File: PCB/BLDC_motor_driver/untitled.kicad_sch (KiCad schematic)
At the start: 21 parts, among them Q8 CSD18533Q5A, Q9 CSD18533Q5A, U1 INA240A2D, U3 IR2104, U4 LMV393

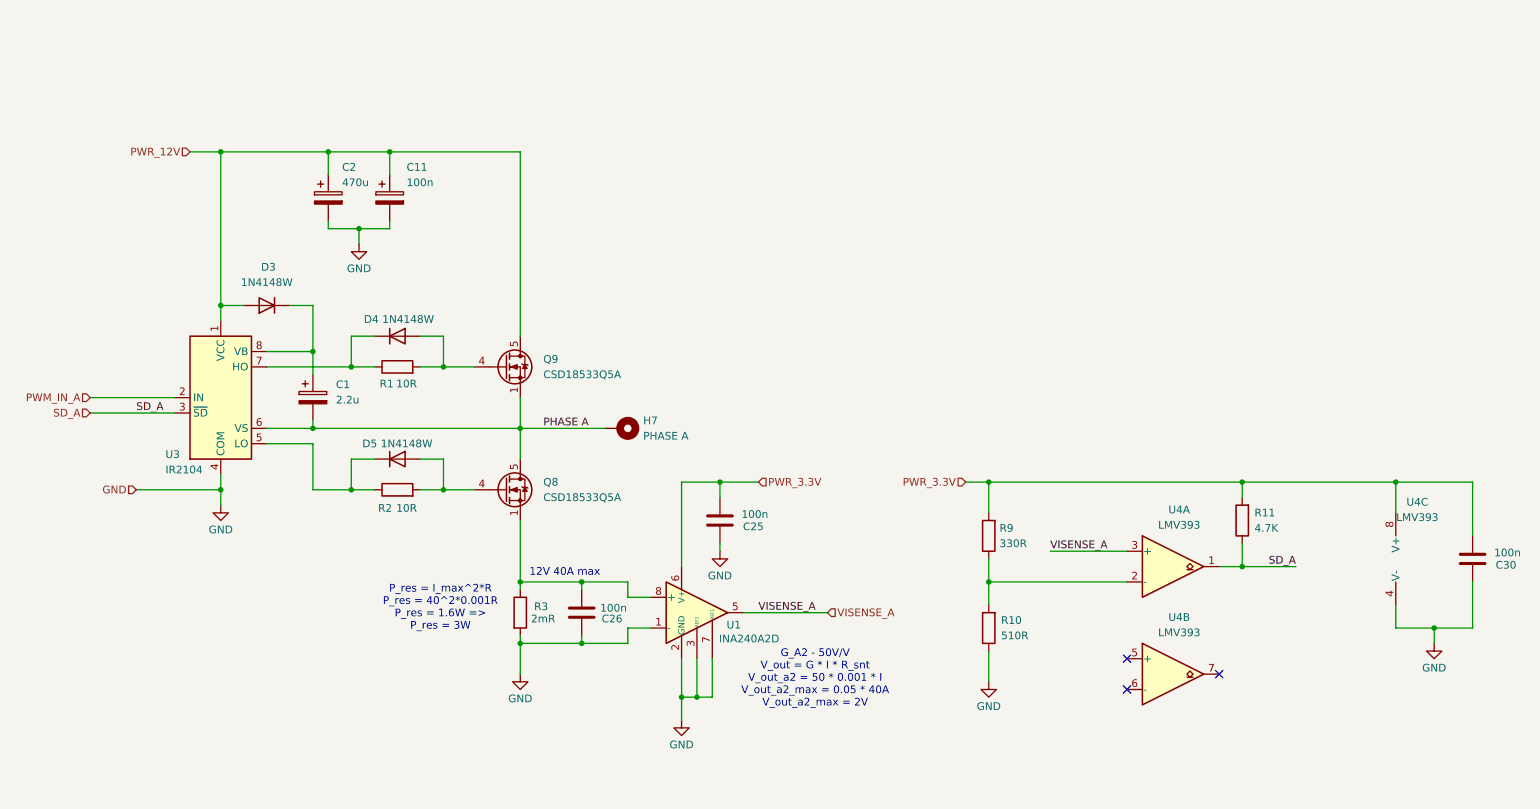
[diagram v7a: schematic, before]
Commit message: Succesfully tested phase alignment with new bldc driver
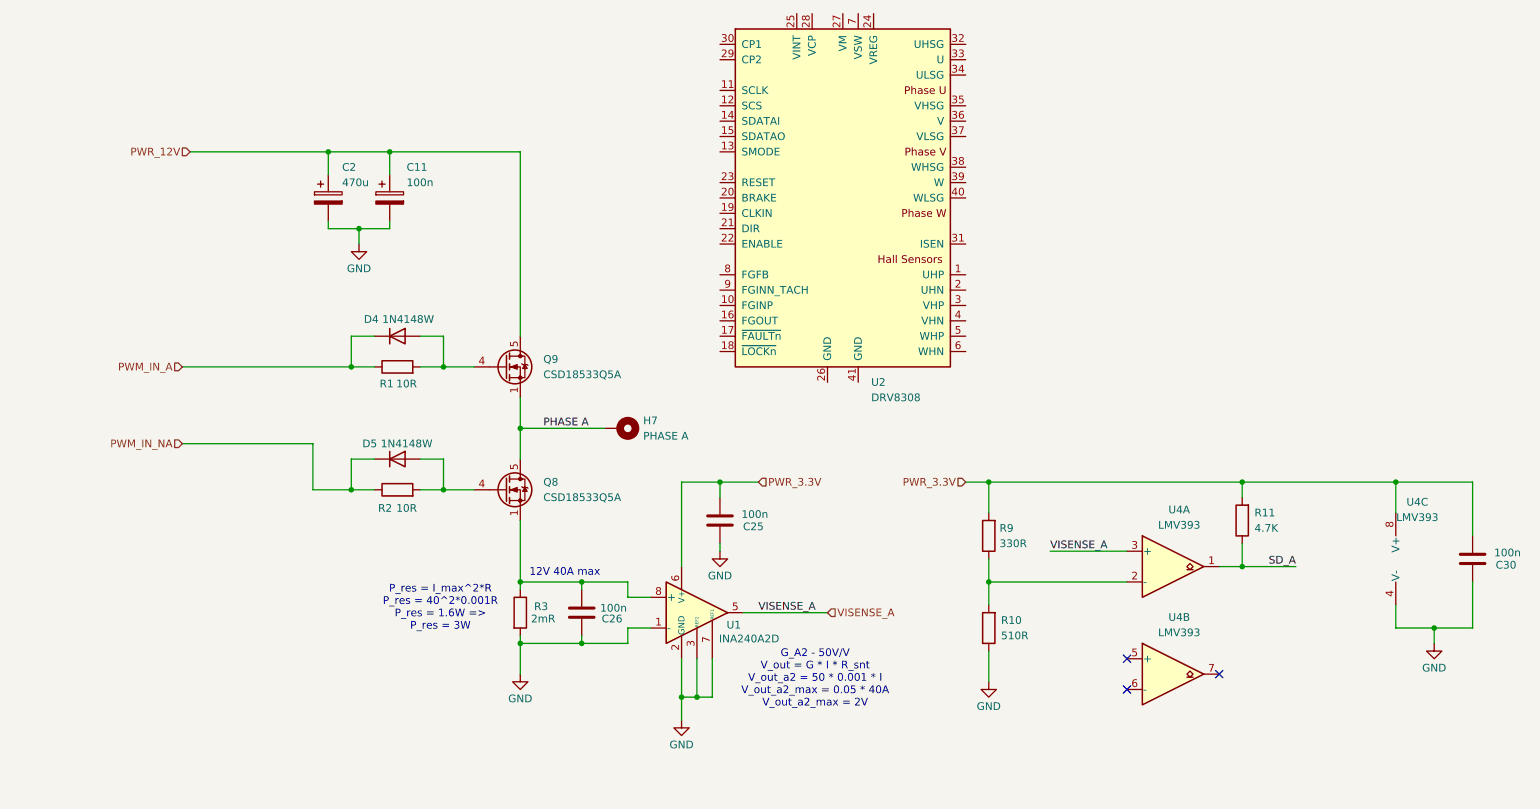
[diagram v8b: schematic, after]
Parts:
- removed C1: 2.2u, Capacitor_Tantalum_SMD:CP_EIA-2012-12_Kemet-R, symbol Device:C_Polarized
- removed D3: 1N4148W, Diode_SMD:D_SOD-123, symbol Diode:1N4148W
- removed U3: IR2104, Package_SO:SOIC-8_3.9x4.9mm_P1.27mm, symbol Driver_FET:IR2104
- added U2: DRV8308, Package_DFN_QFN:Texas_RHA0040E_VQFN-40-1EP_6x6mm_P0.5mm_EP3.52x2.62mm, symbol Driver_Motor:DRV8308
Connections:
- net PWM_IN_A: now also D4.1 (K), R1.1
- net PWM_IN_NA: now reaches D5.1 (K), R2.1
